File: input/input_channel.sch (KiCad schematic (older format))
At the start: 0 parts

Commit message: More work on input board
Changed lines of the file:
@@
 $EndDescr
 $Sheet
-S 7550 3000 1600 1350
+S 6450 3250 1100 550
 U 5DA78AA2
 F0 "ADC" 50
 F1 "adc.sch" 50
+F2 "+in" I L 6450 3350 50
+F3 "-in" I L 6450 3500 50
+F4 "digital" B R 7550 3500 50
 $EndSheet
-Wire Wire Line
-	3150 3350 3400 3350
 $Sheet
-S 5450 3250 1200 500
+S 5100 3250 1050 550
 U 5DE6CDF8
 F0 "antialias_driver" 50
 F1 "antialias_driver.sch" 50
+F2 "in" I L 5100 3350 50
+F3 "-out" I R 6150 3500 50
+F4 "+out" I R 6150 3350 50
+F5 "ref" I L 5100 3500 50
 $EndSheet
 Text Notes 7150 6750 0    50   ~ 0
 One input channel, from filter and protection, all the way through to the ADC.
-Wire Wire Line
-	3150 3500 3400 3500
 $Sheet
-S 1950 3250 1200 550
+S 2150 3250 1200 550
 U 5DE42731
 F0 "in_filter" 50
 F1 "in_filter.sch" 50
-F2 "+out" O R 3150 3350 50
-F3 "-out" O R 3150 3500 50
-F4 "-in" I L 1950 3500 50
-F5 "+in" I L 1950 3350 50
-F6 "BIST_feedback" O R 3150 3700 50
+F2 "+out" O R 3350 3350 50
+F3 "-out" O R 3350 3500 50
+F4 "-in" I L 2150 3500 50
+F5 "+in" I L 2150 3350 50
+F6 "BIST_feedback" O R 3350 3700 50
 $EndSheet
 $Sheet
-S 3400 3000 1600 1050
+S 3700 3250 1100 550
 U 5DA78BF5
 F0 "In amp" 50
 F1 "in_amp.sch" 50
-F2 "-in" I L 3400 3500 50
-F3 "+in" I L 3400 3350 50
-F4 "out" I R 5000 3300 50
-F5 "out_ref" I R 5000 3600 50
+F2 "-in" I L 3700 3500 50
+F3 "+in" I L 3700 3350 50
+F4 "out" I R 4800 3350 50
+F5 "out_ref" I R 4800 3500 50
 $EndSheet
+Wire Wire Line
+	4800 3350 5100 3350
+Wire Wire Line
+	4800 3500 5100 3500
+Wire Wire Line
+	6150 3500 6450 3500
+Wire Wire Line
+	6150 3350 6450 3350
+Wire Wire Line
+	3350 3350 3700 3350
+Wire Wire Line
+	3350 3500 3700 3500
 $EndSCHEMATC

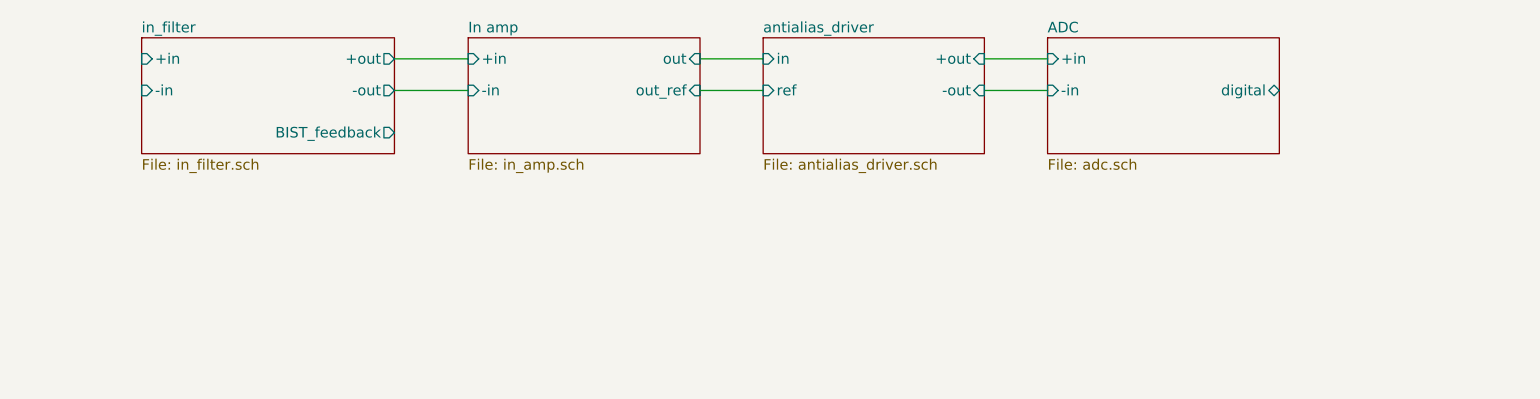
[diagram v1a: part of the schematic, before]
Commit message: Mainly work on the top level of the input board, attaching signals to the channels, digital I/O.  Decided to use Eurocard 64 pin type B connector for the connection to the main board.  See input_board_pinout.txt.
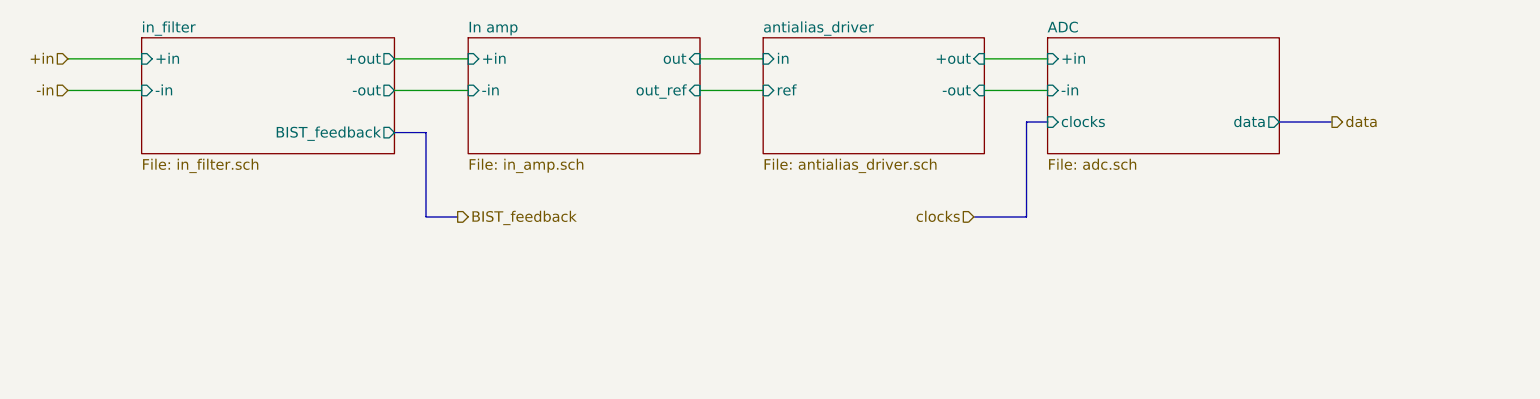
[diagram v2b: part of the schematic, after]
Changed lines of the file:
@@
 EESchema Schematic File Version 4
+LIBS:input_board-cache
 LIBS:input_channel-cache
 EELAYER 29 0
@@
 $Descr A4 11693 8268
 encoding utf-8
-Sheet 1 5
+Sheet 2 10
 Title ""
 Date ""
@@
 F2 "+in" I L 6450 3350 50
 F3 "-in" I L 6450 3500 50
-F4 "digital" B R 7550 3500 50
+F4 "data" O R 7550 3650 50
+F5 "clocks" I L 6450 3650 50
 $EndSheet
 $Sheet
@@
 $Sheet
 S 3700 3250 1100 550
-U 5DA78BF5
+U 5E195558
 F0 "In amp" 50
 F1 "in_amp.sch" 50
@@
 Wire Wire Line
 	3350 3500 3700 3500
+Text HLabel 7800 3650 2    50   Output ~ 0
+data
+Text HLabel 1800 3350 0    50   Input ~ 0
++in
+Text HLabel 1800 3500 0    50   Input ~ 0
+-in
+Wire Wire Line
+	1800 3350 2150 3350
+Wire Wire Line
+	1800 3500 2150 3500
+Text HLabel 3650 4100 2    50   Output ~ 0
+BIST_feedback
+Text HLabel 6100 4100 0    50   Input ~ 0
+clocks
+Wire Bus Line
+	6450 3650 6350 3650
+Wire Bus Line
+	6350 3650 6350 4100
+Wire Bus Line
+	6350 4100 6100 4100
+Wire Bus Line
+	7550 3650 7800 3650
+Wire Bus Line
+	3350 3700 3500 3700
+Wire Bus Line
+	3500 3700 3500 4100
+Wire Bus Line
+	3500 4100 3650 4100
 $EndSCHEMATC

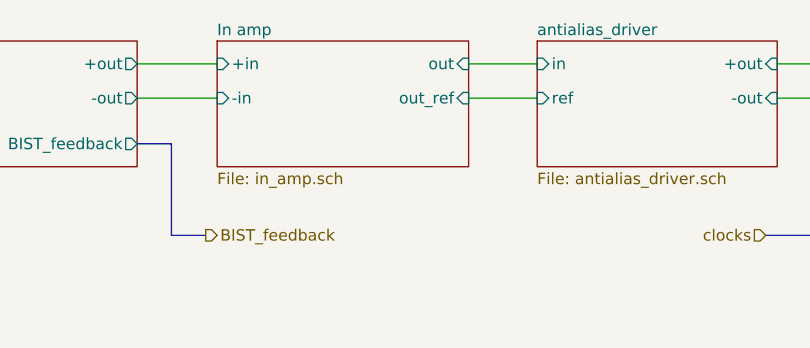
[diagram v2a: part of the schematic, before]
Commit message: Changes mostly related to avoiding excess power consumption.  This is mainly by limiting the signal swing to 0..5V and using asymmetric supplies of -4V and +8V.  (Perhaps we can reduce these to 3/7 V.)  Also, I got rid of two stages in the input signal path.
power_budget.xlsx
power.sch
reference_buffer.sch:
Changes related to the new supply voltages, and start on the power supply section.

input_channel.sch
in_amp.sch
antialias_driver.sch:
Reworked the input signal chain to keep a full differential path, rolling the antialias filter
into the ADC driver.  Also, related to change to lower asymmetrical supply voltages, there is
no 20V PP anywhere (the this was for benefit of the antialias filter noise, but that stage is gone).  Also, added zener clamp on VREF in driver.

in_filter.sch: added missing DC bias resistors.
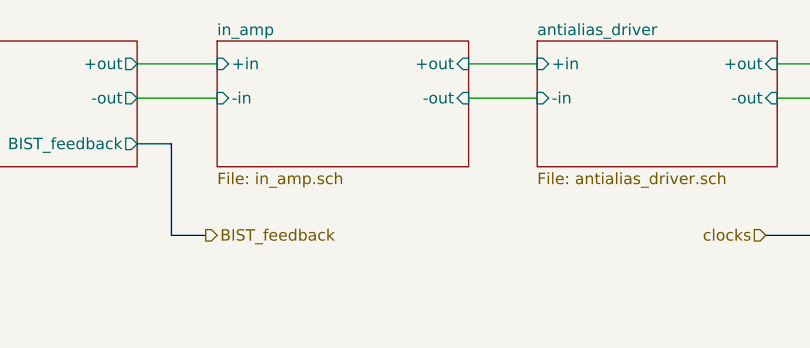
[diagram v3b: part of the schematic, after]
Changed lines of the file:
@@
 LIBS:input_board-cache
 LIBS:input_channel-cache
+LIBS:reference_buffer-cache
 EELAYER 29 0
 EELAYER END
 $Descr A4 11693 8268
 encoding utf-8
-Sheet 2 10
+Sheet 2 11
 Title ""
 Date ""
@@
 F0 "antialias_driver" 50
 F1 "antialias_driver.sch" 50
-F2 "in" I L 5100 3350 50
-F3 "-out" I R 6150 3500 50
-F4 "+out" I R 6150 3350 50
-F5 "ref" I L 5100 3500 50
+F2 "-out" I R 6150 3500 50
+F3 "+out" I R 6150 3350 50
+F4 "-in" I L 5100 3500 50
+F5 "+in" I L 5100 3350 50
 $EndSheet
 Text Notes 7150 6750 0    50   ~ 0
@@
 S 3700 3250 1100 550
 U 5E195558
-F0 "In amp" 50
+F0 "in_amp" 50
 F1 "in_amp.sch" 50
 F2 "-in" I L 3700 3500 50
 F3 "+in" I L 3700 3350 50
-F4 "out" I R 4800 3350 50
-F5 "out_ref" I R 4800 3500 50
+F4 "+out" I R 4800 3350 50
+F5 "-out" I R 4800 3500 50
 $EndSheet
-Wire Wire Line
-	4800 3350 5100 3350
-Wire Wire Line
-	4800 3500 5100 3500
 Wire Wire Line
 	6150 3500 6450 3500
@@
 Wire Bus Line
 	3500 4100 3650 4100
+Wire Wire Line
+	4800 3350 5100 3350
+Wire Wire Line
+	4800 3500 5100 3500
 $EndSCHEMATC

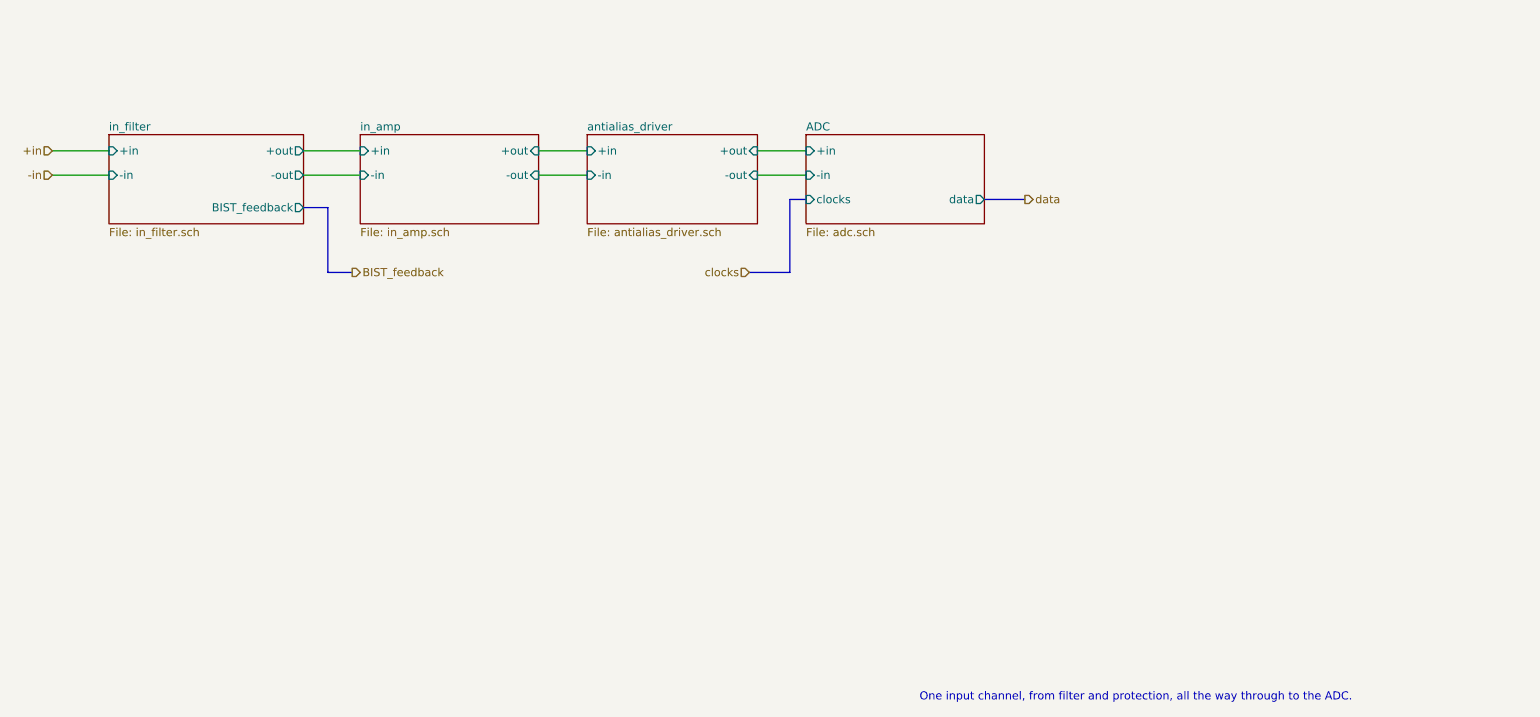
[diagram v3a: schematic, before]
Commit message: Mostly work on power, regulators and distribution.  Also more BOM cleanup.
All of the bypass capacitors are now spec'd and in the DigiKey BOM. TVS zeners are now
spec'd.  Folded together some resistor values and got rid of some 1206 parts that no longer
need that much power rating at the lower supplies.

A affecting all of the input channel sheets is that we now distribute filtered V+, V- and VREF
via sheet ports.  The V+, V- filter is on input_channel.sch and the VREF filter is still in
adc.sch, but is distributed out to the other sheets that need it.

bist_buffer.sch: added buffer for built-in self-test

board_connector.sch: put the input filter for the analog supplies here.

power.sch: added regulators for the supplies.

reference_buffer.sch:
changed components to match those chosen for the V+, V- regulators and added
current steering diodes to bootstrap the reference buffer supply.  This is
necessary because the analog supplies are now derived from VREF.

*.wxsch:
Updates to spice models related to work on supplies.
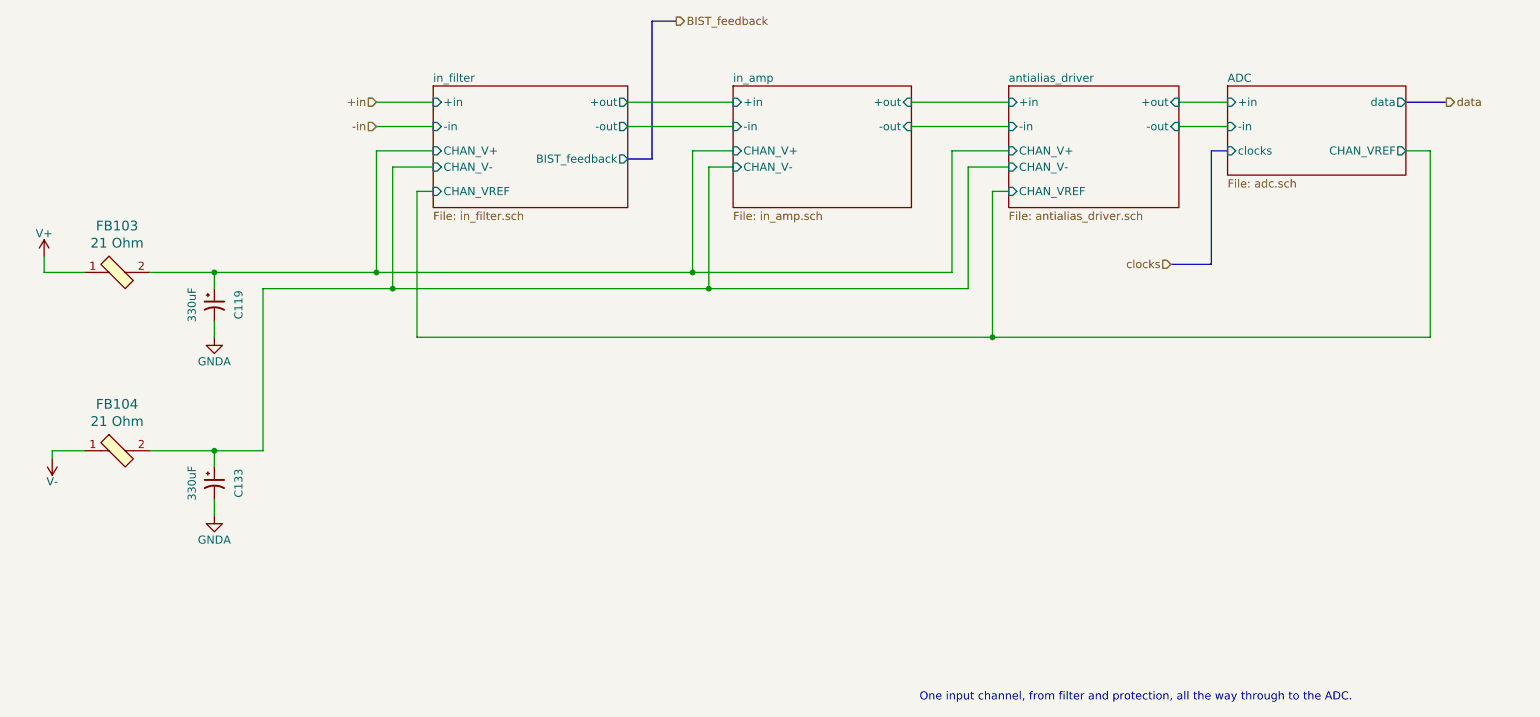
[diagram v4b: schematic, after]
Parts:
- added C119, C133: 330uF, Capacitor_SMD:CP_Elec_8x6.7, symbol Device:CP1_Small
- added FB103, FB104: 21 Ohm, digikey-footprints:0805, symbol dk_Ferrite-Beads-and-Chips:MPZ2012S601AT000
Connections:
- new net GNDA: C119.2, C133.2
- new net V+: FB103.1
- new net V-: FB104.1
- new net antialias_driver/CHAN_V+: C119.1, FB103.2
- new net antialias_driver/CHAN_V-: C133.1, FB104.2
